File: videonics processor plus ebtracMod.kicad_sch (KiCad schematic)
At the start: 0 parts

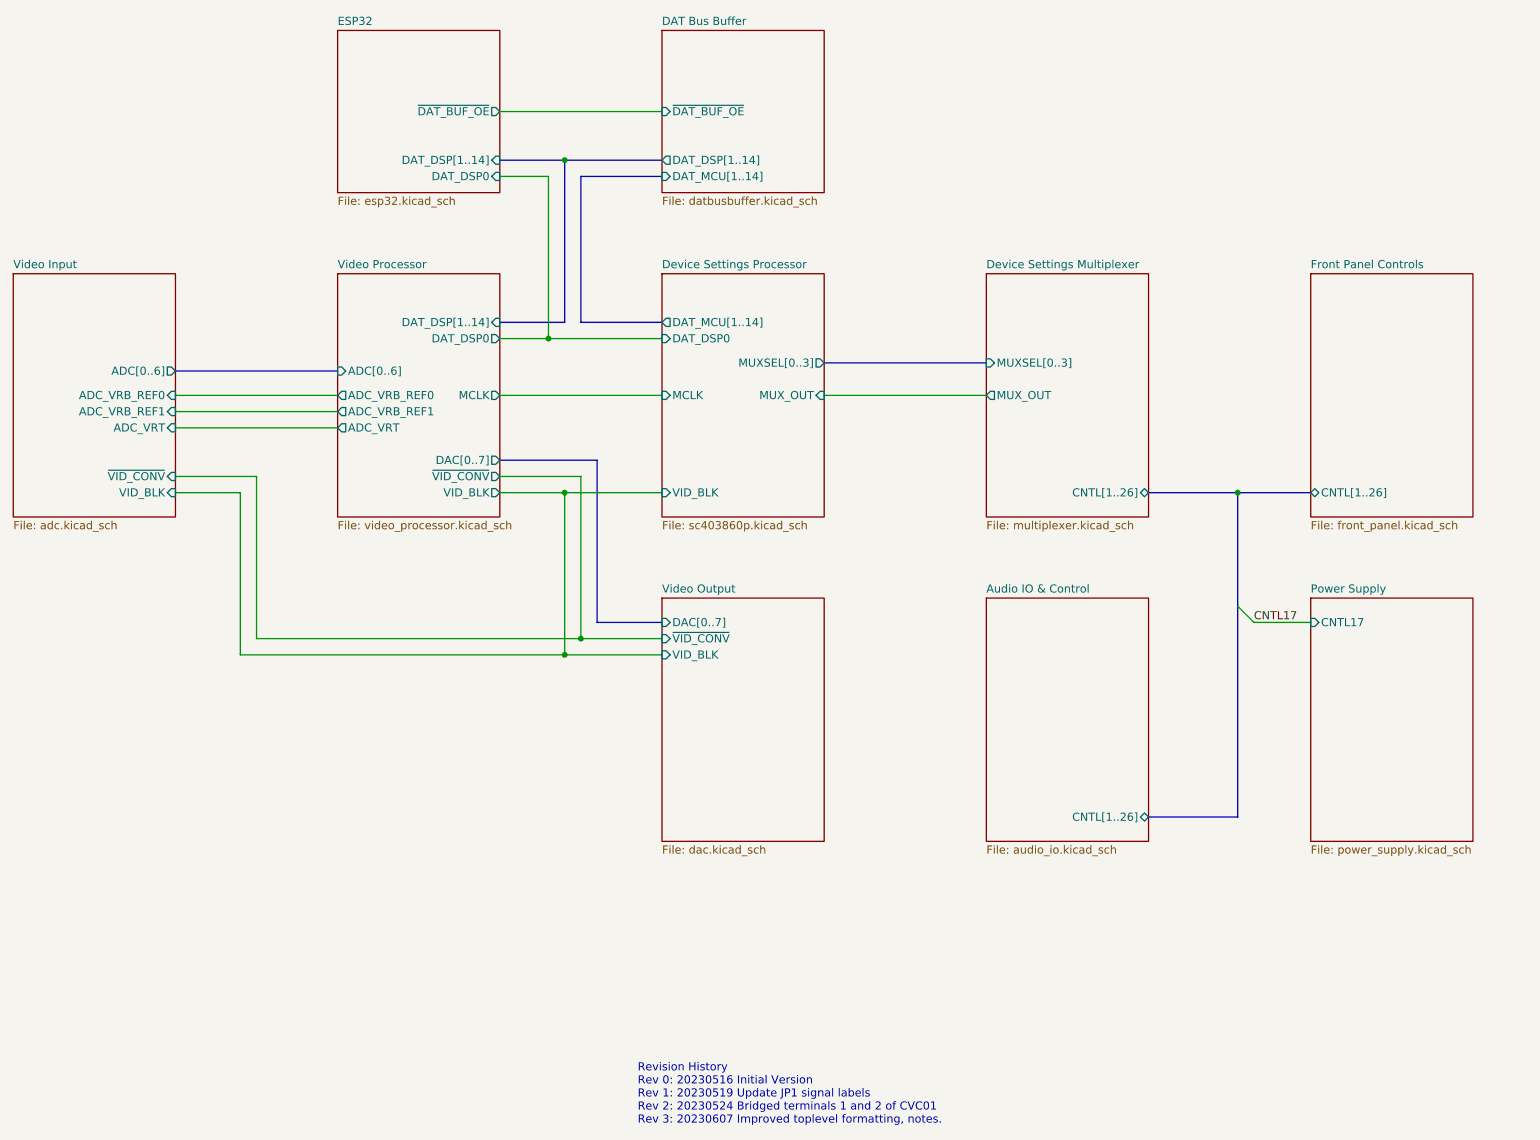
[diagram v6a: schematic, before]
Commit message: cleanup and rename subsheets, increment rev
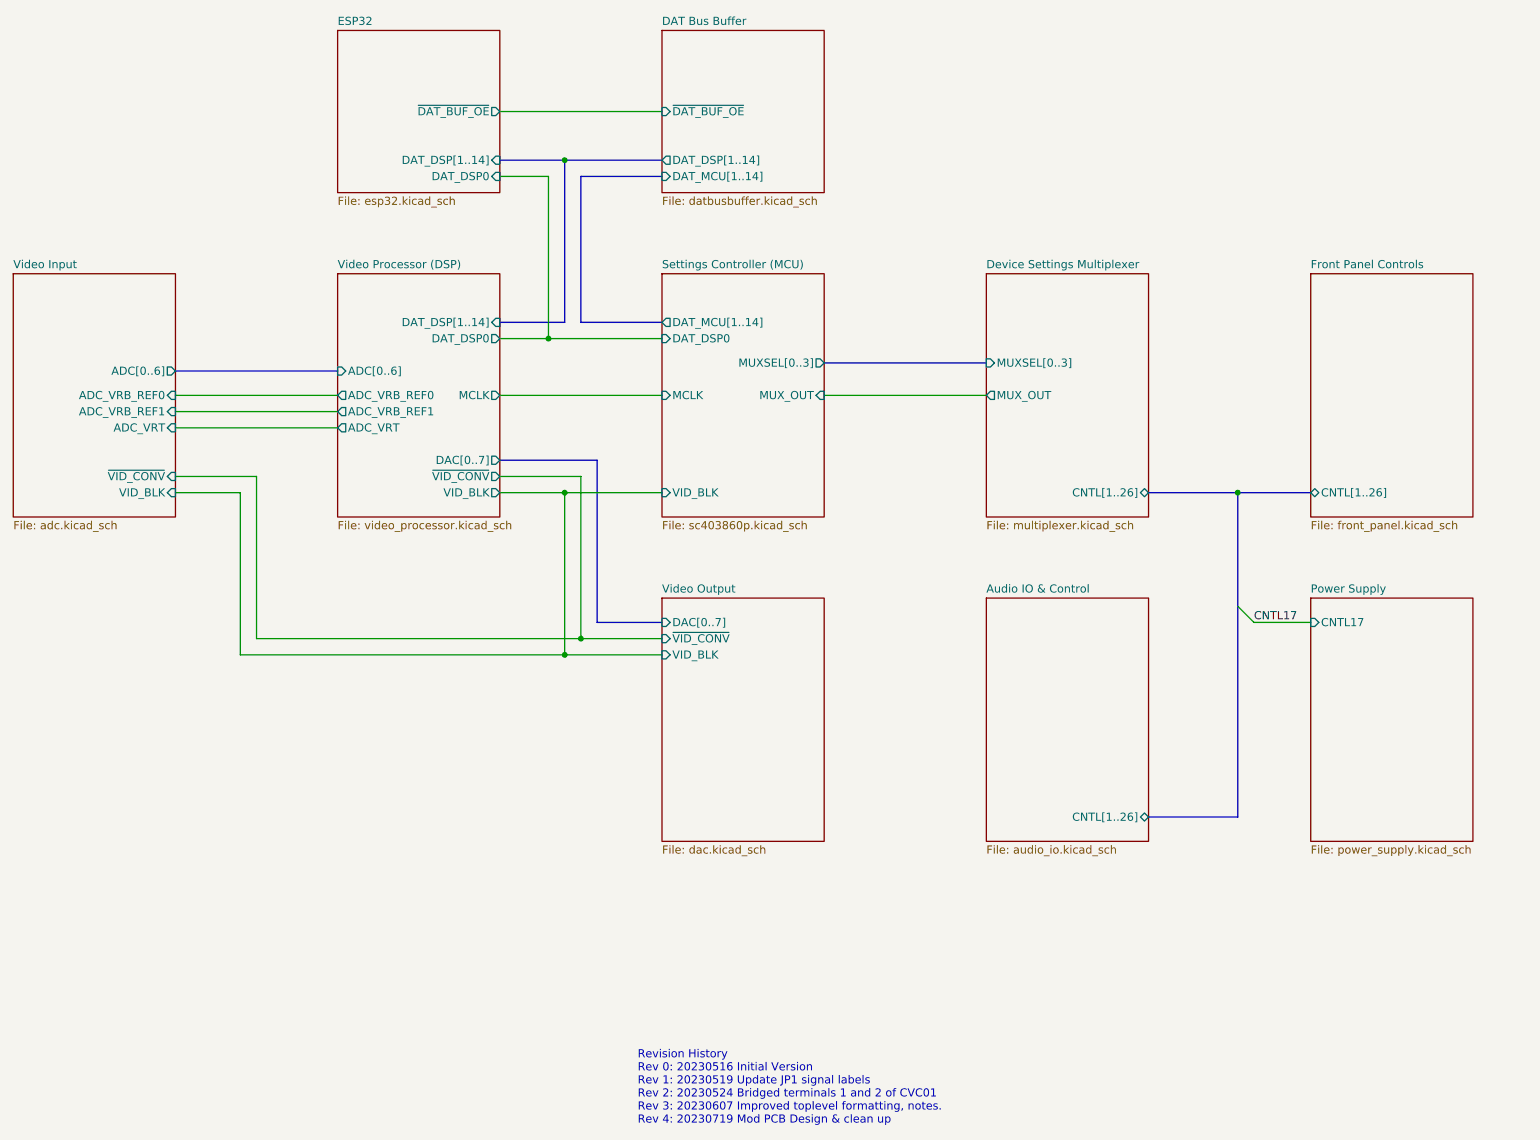
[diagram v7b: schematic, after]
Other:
- sheet Device Settings Processor renamed Settings Controller (MCU)
- sheet Video Processor renamed Video Processor (DSP)
- note added: "Revision History Rev 0: 20230516 Initial Version Rev 1: 20230519 Update JP1 signal labels Rev 2: 20230524 Bridged terminals 1 and 2 of CVC01 Rev 3: 20230607 Improved toplevel formatting, notes. Rev 4: 20230719 Mod PCB Design & clean up"
- note removed: "Revision History Rev 0: 20230516 Initial Version Rev 1: 20230519 Update JP1 signal labels Rev 2: 20230524 Bridged terminals 1 and 2 of CVC01 Rev 3: 20230607 Improved toplevel formatting, notes."
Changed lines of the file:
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@@
   (title_block
     (title "Videonics Processor Plus PP-1 NTSC - Modded")
-    (date "2023-05-24")
-    (rev "3")
+    (date "2023-07-19")
+    (rev "4")
     (company "E Tracy")
   )
@@
     (stroke (width 0) (type default) (color 0 0 0 0))
   )
-  (text "Revision History\nRev 0: 20230516 Initial Version\nRev 1: 20230519 Update JP1 signal labels\nRev 2: 20230524 Bridged terminals 1 and 2 of CVC01\nRev 3: 20230607 Improved toplevel formatting, notes."
+  (text "Revision History\nRev 0: 20230516 Initial Version\nRev 1: 20230519 Update JP1 signal labels\nRev 2: 20230524 Bridged terminals 1 and 2 of CVC01\nRev 3: 20230607 Improved toplevel formatting, notes.\nRev 4: 20230719 Mod PCB Design & clean up"
     (at 123.19 196.85 0)
     (effects (font (size 1.27 1.27)) (justify left bottom))
@@
     (stroke (width 0.1524) (type solid) (color 0 0 0 0))
     (fill (color 255 229 191 1.0000))
-    (property "Sheet name" "Device Settings Processor" (id 0) (at 127 62.7884 0)
+    (property "Sheet name" "Settings Controller (MCU)" (id 0) (at 127 62.7884 0)
       (effects (font (size 1.27 1.27)) (justify left bottom))
     )
@@
     (stroke (width 0.1524) (type solid) (color 0 0 0 0))
     (fill (color 255 229 191 1.0000))
-    (property "Sheet name" "Video Processor" (id 0) (at 76.2 62.7884 0)
-      (effects (font (size 1.27 1.27)) (justify left bottom))
-    )
+    (property "Sheet name" "Video Processor (DSP)" (id 0) (at 76.2 62.7884 0)
+      (effects (font (size 1.27 1.27)) (justify left bottom))
+    )
